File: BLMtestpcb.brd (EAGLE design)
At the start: 105 x 87 mm, 92 parts, among them IC1 NTB0102DP, IC10 PIC16F18325-I/P, IC11 MAX11644EUA+, IC4 PIC24F16KA301-I/SS,, IC5 NE555D, IC6 MULTIPLEX1, IC7 AD623R, IC8 AD822R, IC9 AD623R, Q3 12MHz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

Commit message: Update to V1.1
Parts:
- JP1: value Distance Select 0B -> Type select 0
- JP2: value Type Select 0 -> Setup select 0
- JP4: value Distance Select 0A -> Type select 0
- JP5: value Type Select 1 -> Setup select 1
- JP6: value Distance Select 1A -> Type select 1
- JP9: value Distance Select 1B -> Type select 1
- moved H2 4.12 mm to (65.0, 5.00)
- moved PHDA1 2.50 mm to (79.5, 50.0)
- moved PHDA2 2.50 mm to (82.0, 50.0)
- moved H1 1.00 mm to (5.00, 5.00)
- moved JP18 0.51 mm to (4.01, 67.0)
- turned JP1 to 90 degrees
- turned JP4 to 90 degrees
- turned JP5 to 270 degrees
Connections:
- net 0A_CLOSE renamed TYPE00A
- net 0B_FAR renamed TYPE01B
- net 1A_FAR renamed TYPE10A
- net 1B_FAR renamed TYPE11B
- net BPW34_2 renamed BOT1
- net N$1 renamed OP-AMP1
- net N$35 renamed OP-AMP0
- net SFH_2700 renamed TOP0
- removed net 0A_FAR: JP4.1, PHDA2.1, PHDA2.2
- removed net 0B_CLOSE: JP1.3, PHDB1.A
- removed net 1A_CLOSE: JP6.1, PHDA3.1, PHDA3.2
- removed net 1B_CLOSE: JP9.3, PHDB4.A
- removed net BPW34: JP2.3, JP4.2
- removed net SFH_2700_2: JP5.1, JP9.2
- new net BOT0: JP2.3, JP9.2
- new net TOP1: JP4.2, JP5.1
- new net TYPE00B: JP4.1, PHDB1.A
- new net TYPE01A: JP1.3, PHDA2.1, PHDA2.2
- new net TYPE10B: JP6.1, PHDB4.A
- new net TYPE11A: JP9.3, PHDA3.1, PHDA3.2
- net +3.3V: now also IC1.6
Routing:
- net TYPE00B: track 0.00 -> 52.7 mm
- net TYPE10B: track 0.00 -> 51.9 mm, vias 0 -> 2
- net BOT0: track 0.00 -> 45.5 mm
- net BPW34: track 37.7 -> 0.00 mm
- net SFH_2700_2: track 35.8 -> 0.00 mm
- net 1B_CLOSE: track 34.5 -> 0.00 mm
- net 0B_CLOSE: track 31.3 -> 0.00 mm
- net TOP1: track 0.00 -> 28.8 mm
- net TYPE11A: track 0.00 -> 27.0 mm
- net TYPE01A: track 0.00 -> 26.5 mm, vias 0 -> 2
- net 1A_CLOSE: track 23.3 -> 0.00 mm
- net 0A_FAR: track 19.3 -> 0.00 mm
- net BOT1: track 37.6 -> 27.6 mm
- net TYPE00A: track 26.3 -> 19.1 mm
- net TOP0: track 35.7 -> 30.1 mm
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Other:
- board text added: "BOTTOM"
- board text added: "IPD Blood Monitor Sensor Test PCB V1.1"
- board text added: "TOP"
- board text added: "TYPE A"
- board text added: "TYPE B"
- board text removed: "BPW34"
- board text removed: "CLOSE"
- board text removed: "FAR"
- board text removed: "IPD Blood Monitor Sensor Test PCB V1"
- board text removed: "SFH 2700"

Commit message: Update to v1.2
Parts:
- JP1, JP4: value Type select 0 -> Diode select 0
- JP13: value ADC select 0 -> ADC select
- JP14: value ADC select 1 -> ADC select
- JP2: value Setup select 0 -> Setup select
- JP20: value LED Select A -> LED Select 940
- JP21: value LED Select B -> LED Select 850
- JP22: value LED Select C -> LED Select 660
- JP5: value Setup select 1 -> Setup select
- JP6, JP9: value Type select 1 -> Diode select 1
- moved JP9 8.50 mm to (61.1, 38.8)
- moved JP5 7.21 mm to (64.9, 70.4)
- moved JP14 5.83 mm to (46.7, 48.8)
- moved JP1 5.38 mm to (64.8, 50.1)
- moved JP13 4.12 mm to (46.8, 52.8)
- moved JP6 3.92 mm to (65.1, 38.8)
- moved JP4 3.62 mm to (60.8, 50.1)
- moved JP2 3.00 mm to (60.9, 70.5)
- moved C2 1.42 mm to (15.3, 62.1)
- moved C8 1.32 mm to (16.0, 30.2)
- moved C16 0.80 mm to (13.1, 38.0)
- moved C15 0.59 mm to (8.90, 34.6)
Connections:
- net N$27 renamed 940A
- net N$28 renamed 940B
- net N$29 renamed 850A
- net N$30 renamed 850B
- net N$31 renamed 660A
- net N$32 renamed 660B
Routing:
- net SDA1: track 49.4 -> 35.8 mm
- net BOT0: track 45.5 -> 32.8 mm
- net BOT1: track 27.6 -> 37.7 mm
- net TOP0: track 30.1 -> 38.8 mm
- net RC3: track 35.5 -> 28.1 mm
- net TYPE01A: track 26.5 -> 19.6 mm, vias 2 -> 0
- net TYPE10A: track 22.9 -> 19.1 mm
- net OP-AMP1: track 59.7 -> 63.4 mm
- net RC2: track 28.8 -> 32.2 mm
- net OP-AMP0: track 13.1 -> 9.87 mm
- net ADCIN0: track 38.6 -> 41.8 mm
- net TYPE10B: track 51.9 -> 49.5 mm, vias 2 -> 0
- net TYPE00A: track 19.1 -> 21.0 mm
- net ADCIN1: track 54.3 -> 56.1 mm
- net TYPE01B: track 42.8 -> 41.2 mm
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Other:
- board text added: "A"
- board text added: "B"
- board text added: "BOT"
- board text added: "GND"
- board text added: "IPD Blood Monitor Sensor Test PCB V1_2"
- board text removed: "BOTTOM"
- board text removed: "G"
- board text removed: "IPD Blood Monitor Sensor Test PCB V1.1"

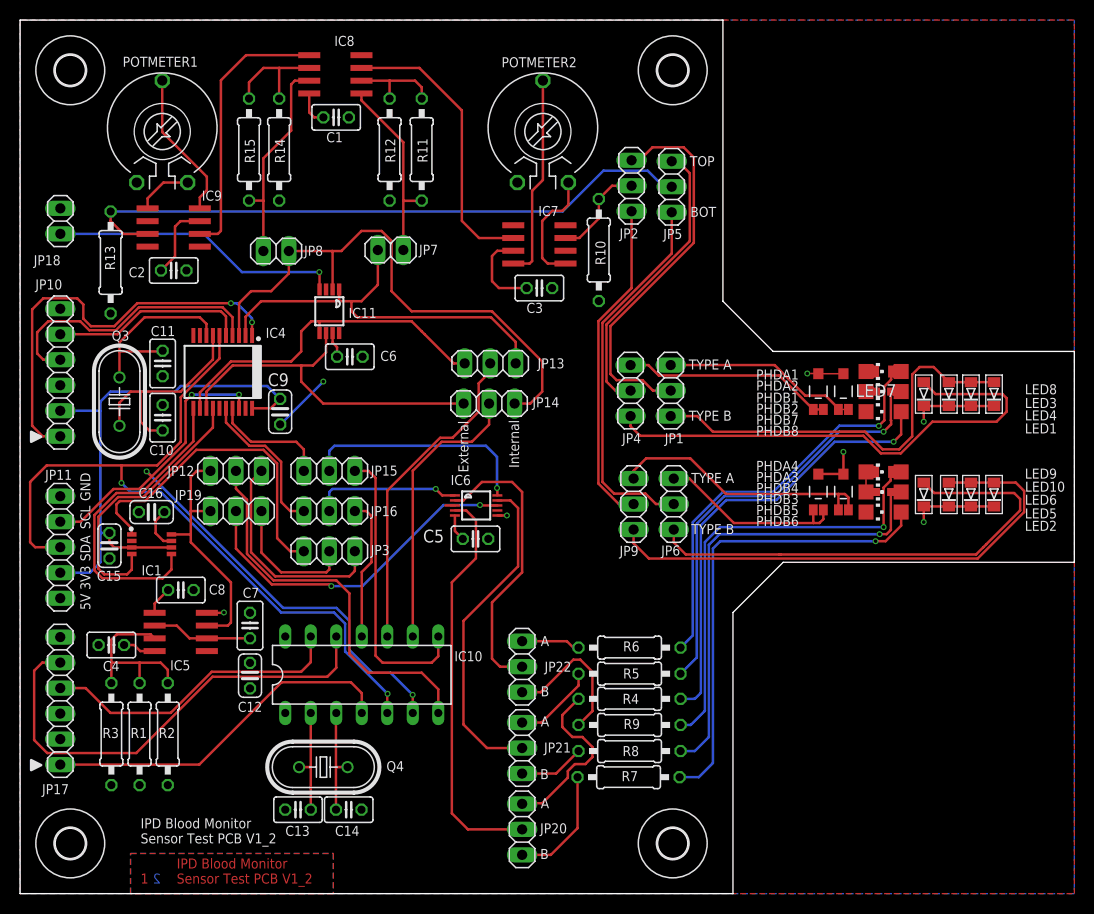
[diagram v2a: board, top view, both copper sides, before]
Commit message: Update to v1_3
Change some component footprints to have pin 1 indication. Remove 1mm length difference in PCB
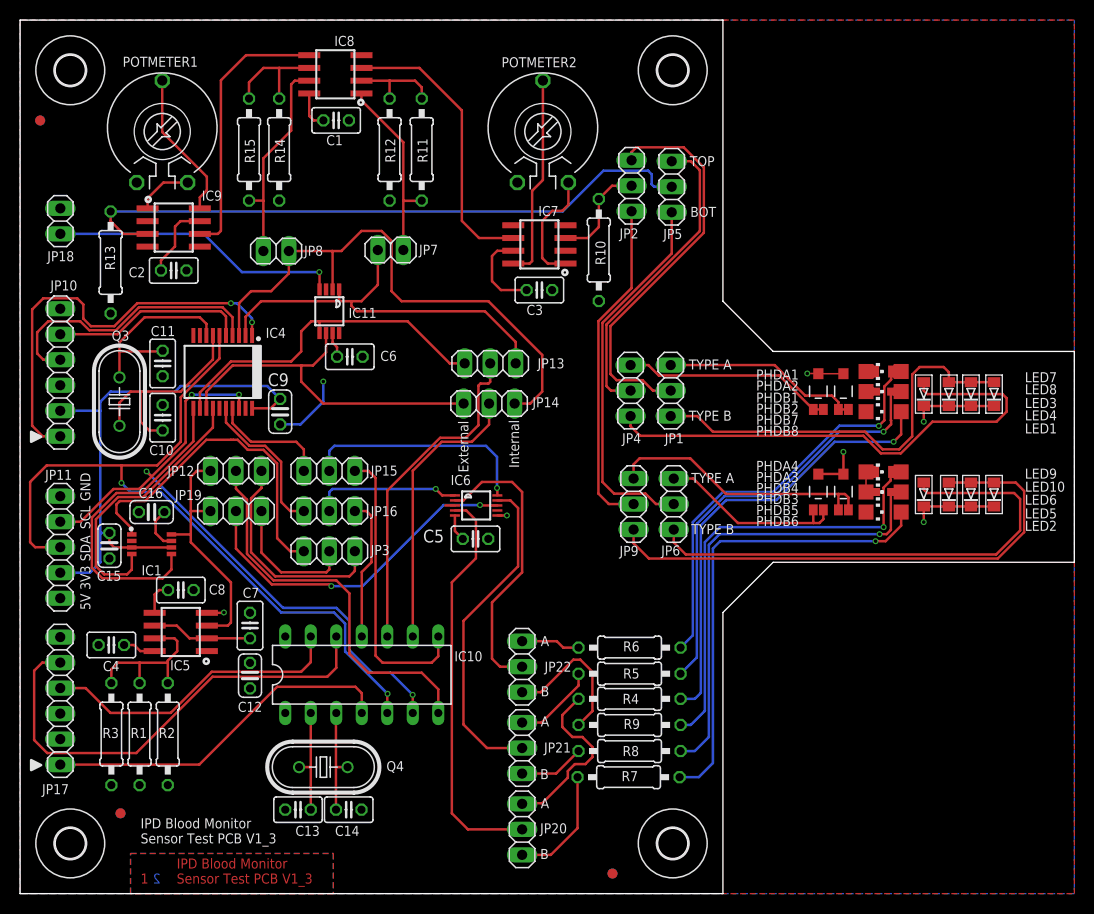
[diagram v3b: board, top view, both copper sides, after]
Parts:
- added U$1, U$2, U$3, U$4, U$5, U$6: FIDUCIAL, adafruit:FIDUCIAL_1MM
- IC5: device linear:SO08 -> linear_custom:SO08
- IC7, IC8, IC9: device analog-devices:SO8 -> analog-devices_custom:SO8
- moved C1 0.30 mm to (31.5, 77.0)
- moved C3 0.20 mm to (51.7, 60.1)
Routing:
- net N$15: track 18.3 -> 16.2 mm
- net TOP1: track 29.3 -> 31.1 mm
- net TYPE10B: track 49.5 -> 51.1 mm
- net TOP0: track 38.8 -> 40.1 mm
- net RC2: track 32.2 -> 33.4 mm
- net GND: track 9.02 -> 10.2 mm
- net TYPE11B: track 52.8 -> 53.9 mm
- net PWMUC2: track 33.1 -> 33.9 mm
- net TYPE01B: track 41.2 -> 41.8 mm
- net OP-AMP1: track 63.4 -> 64.0 mm
- net BOT0: track 32.8 -> 33.4 mm
- net N$17: track 2.83 -> 3.35 mm
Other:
- outline, holes or cut-outs redrawn
- board text added: "IPD Blood Monitor Sensor Test PCB V1_3"
- board text removed: "IPD Blood Monitor Sensor Test PCB V1_2"
